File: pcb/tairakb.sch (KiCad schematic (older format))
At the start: 79 parts, among them SW1 SW_Push, SW10 SW_Push, SW11 SW_Push, SW12 SW_Push, SW13 SW_Push, SW14 SW_Push, SW15 SW_Push, SW16 SW_Push, SW17 SW_Push, SW18 SW_Push, SW19 SW_Push, SW2 SW_Push, SW20 SW_Push, SW20-1 SW_Push, SW21 SW_Push, SW22 SW_Push, SW23 SW_Push, SW24 SW_Push, SW25 SW_Push, SW26 SW_Push, SW27 SW_Push, SW28 SW_Push, SW29 SW_Push, SW3 SW_Push, SW30 SW_Push, SW31 SW_Push, SW32 SW_Push, SW33 SW_Push, SW4 SW_Push, SW5 SW_Push, SW6 SW_Push, SW7 SW_Push, SW8 SW_Push, SW9 SW_Push, U3 nice!nano

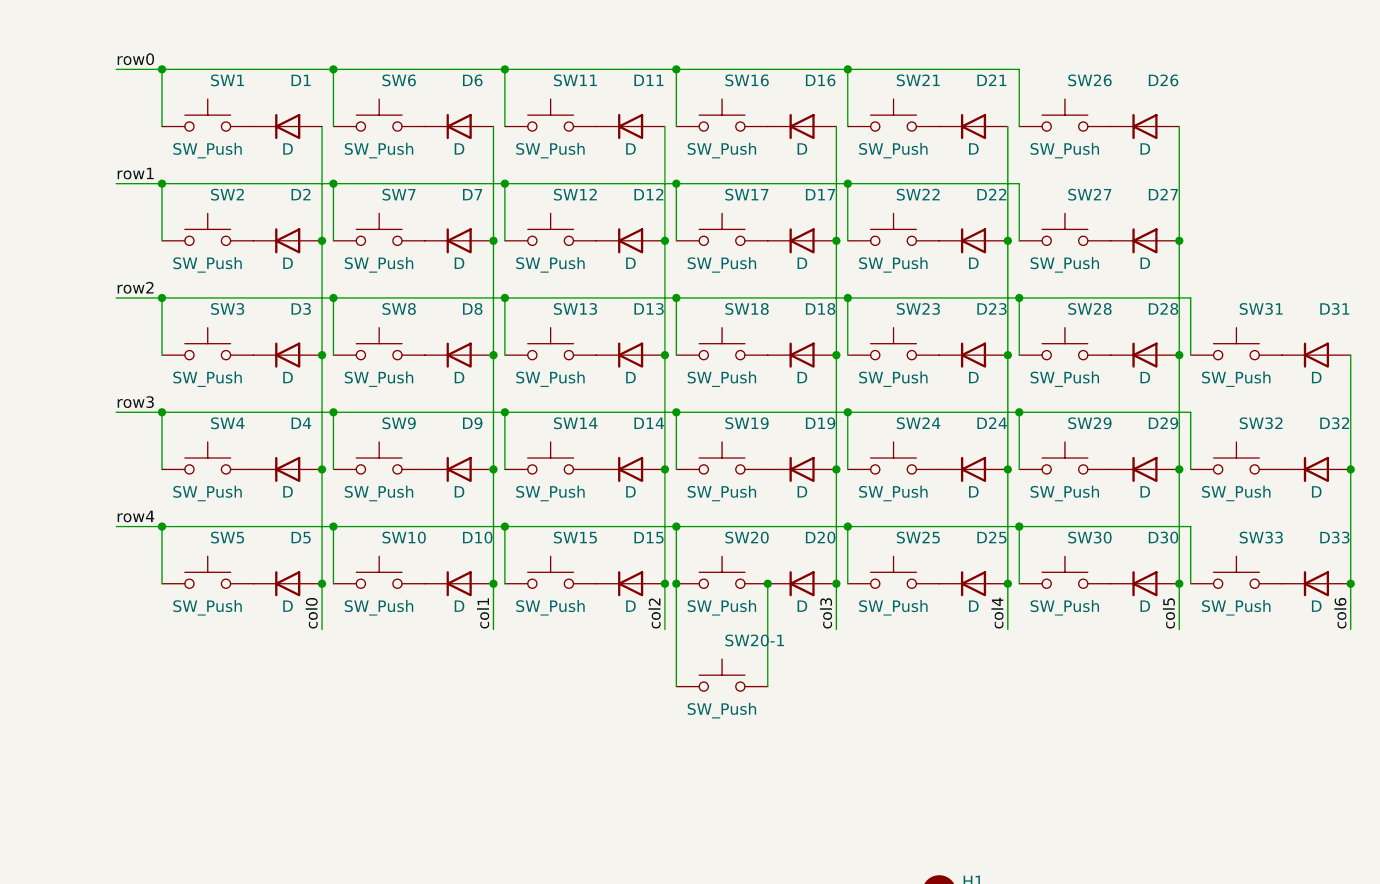
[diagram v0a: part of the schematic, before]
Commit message: Add traces routed by hand
Previously the diodes were connected from the columns to the switches.
Both the ErgoDash and the Corne have them behind the switches connected
to the rows. Since I positioned the diodes on the PCB like they are in
the ErgoDash and Corne, the routing was much more difficult than intended.

This moves the diodes behind the switches and also moves them around a
bit on the PCB. This allowed me to hand route all traces easily, so this
time no autorouter has been involved.

The via count is rather large (156). I opted to rather have ONE trace
and then interconnect each component with vias itself. An alternative
could be to run traces for rows and columns on both layers, but then
there still would be a lot of conflicting paths requiring vias anyway.

I also removed both GND zones. There is nothing on the board that needs
ground except the nice!nano and the battery and I didn't want to start
adding complicated routing just to get GND zones on the whole board. I
left one GND zone in the nice!nano area since it seems reasonable there.
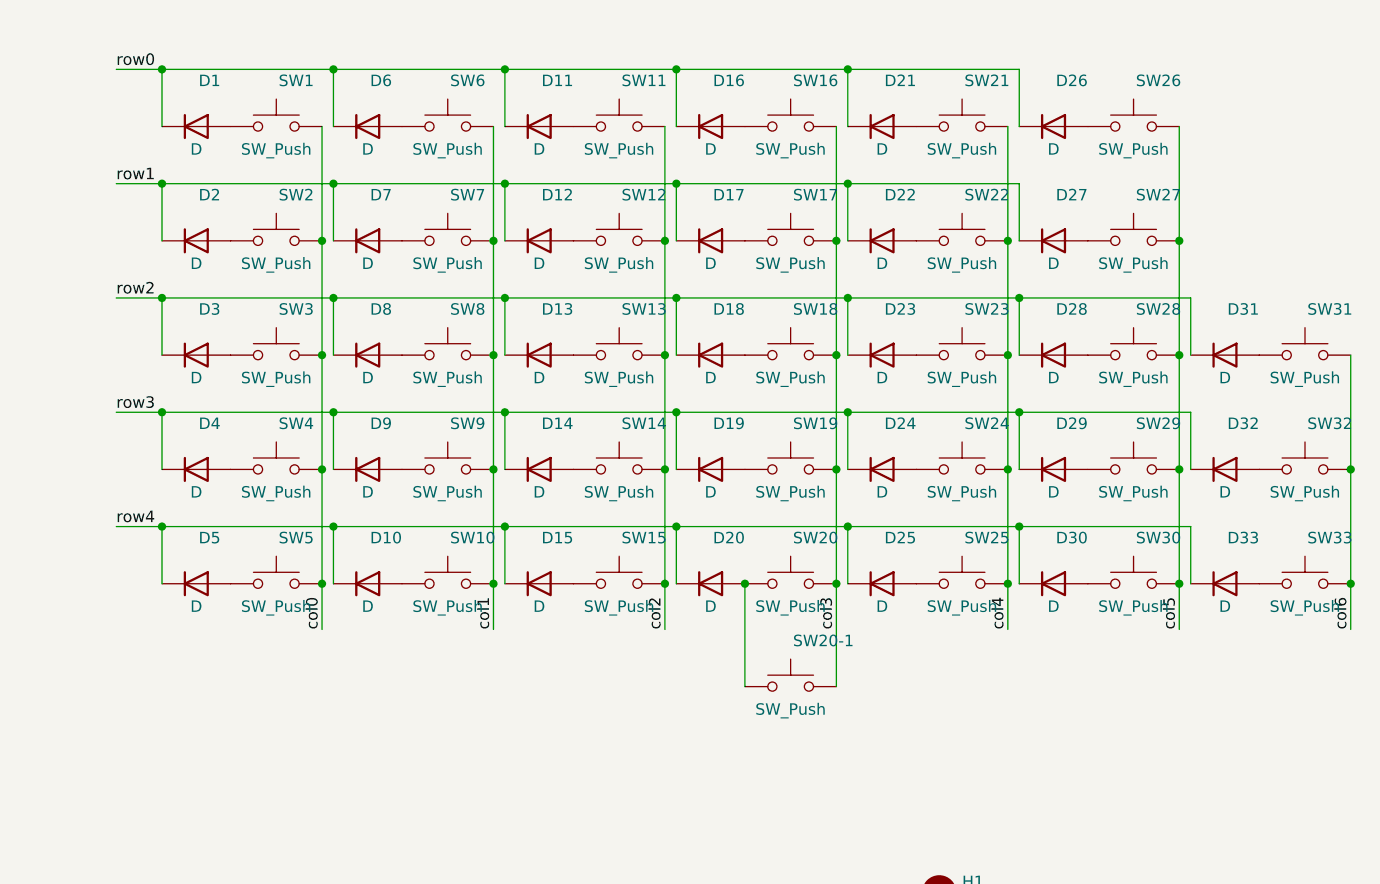
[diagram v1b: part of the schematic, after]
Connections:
- net col0: now also SW1.2, SW2.2, SW3.2, SW4.2, SW5.2; no longer D1.2 (A), D2.2 (A), D3.2 (A), D4.2 (A), D5.2 (A)
- net col1: now also SW10.2, SW6.2, SW7.2, SW8.2, SW9.2; no longer D10.2 (A), D6.2 (A), D7.2 (A), D8.2 (A), D9.2 (A)
- net col2: now also SW11.2, SW12.2, SW13.2, SW14.2, SW15.2; no longer D11.2 (A), D12.2 (A), D13.2 (A), D14.2 (A), D15.2 (A)
- net col3: now also SW16.2, SW17.2, SW18.2, SW19.2, SW20-1.2, SW20.2; no longer D16.2 (A), D17.2 (A), D18.2 (A), D19.2 (A), D20.2 (A)
- net col4: now also SW21.2, SW22.2, SW23.2, SW24.2, SW25.2; no longer D21.2 (A), D22.2 (A), D23.2 (A), D24.2 (A), D25.2 (A)
- net col5: now also SW26.2, SW27.2, SW28.2, SW29.2, SW30.2; no longer D26.2 (A), D27.2 (A), D28.2 (A), D29.2 (A), D30.2 (A)
- net col6: now also SW31.2, SW32.2, SW33.2; no longer D31.2 (A), D32.2 (A), D33.2 (A)
- net row0: now also D1.1 (K), D11.1 (K), D16.1 (K), D21.1 (K), D26.1 (K), D6.1 (K); no longer SW1.1, SW11.1, SW16.1, SW21.1, SW26.1, SW6.1
- net row1: now also D12.1 (K), D17.1 (K), D2.1 (K), D22.1 (K), D27.1 (K), D7.1 (K); no longer SW12.1, SW17.1, SW2.1, SW22.1, SW27.1, SW7.1
- net row2: now also D13.1 (K), D18.1 (K), D23.1 (K), D28.1 (K), D3.1 (K), D31.1 (K), D8.1 (K); no longer SW13.1, SW18.1, SW23.1, SW28.1, SW3.1, SW31.1, SW8.1
- net row3: now also D14.1 (K), D19.1 (K), D24.1 (K), D29.1 (K), D32.1 (K), D4.1 (K), D9.1 (K); no longer SW14.1, SW19.1, SW24.1, SW29.1, SW32.1, SW4.1, SW9.1
- net row4: now also D10.1 (K), D15.1 (K), D20.1 (K), D25.1 (K), D30.1 (K), D33.1 (K), D5.1 (K); no longer SW10.1, SW15.1, SW20-1.1, SW20.1, SW25.1, SW30.1, SW33.1, SW5.1
- new net: D1.2 (A), SW1.1
- new net: D6.2 (A), SW6.1
- new net: D11.2 (A), SW11.1
- new net: D16.2 (A), SW16.1
- new net: D21.2 (A), SW21.1
- new net: D26.2 (A), SW26.1
- new net: D2.2 (A), SW2.1
- new net: D7.2 (A), SW7.1
- new net: D12.2 (A), SW12.1
- new net: D17.2 (A), SW17.1
- new net: D22.2 (A), SW22.1
- new net: D27.2 (A), SW27.1
- new net: D3.2 (A), SW3.1
- new net: D8.2 (A), SW8.1
- new net: D13.2 (A), SW13.1
- new net: D18.2 (A), SW18.1
- new net: D23.2 (A), SW23.1
- new net: D28.2 (A), SW28.1
- new net: D31.2 (A), SW31.1
- new net: D4.2 (A), SW4.1
- new net: D9.2 (A), SW9.1
- new net: D14.2 (A), SW14.1
- new net: D19.2 (A), SW19.1
- new net: D24.2 (A), SW24.1
- new net: D29.2 (A), SW29.1
- new net: D32.2 (A), SW32.1
- new net: D5.2 (A), SW5.1
- new net: D10.2 (A), SW10.1
- new net: D15.2 (A), SW15.1
- new net: D20.2 (A), SW20-1.1, SW20.1
- new net: D25.2 (A), SW25.1
- new net: D30.2 (A), SW30.1
- new net: D33.2 (A), SW33.1
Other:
- moved on the sheet: D1, D10, D11, D12, D13, D14, D15, D16, D17, D18, D19, D2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

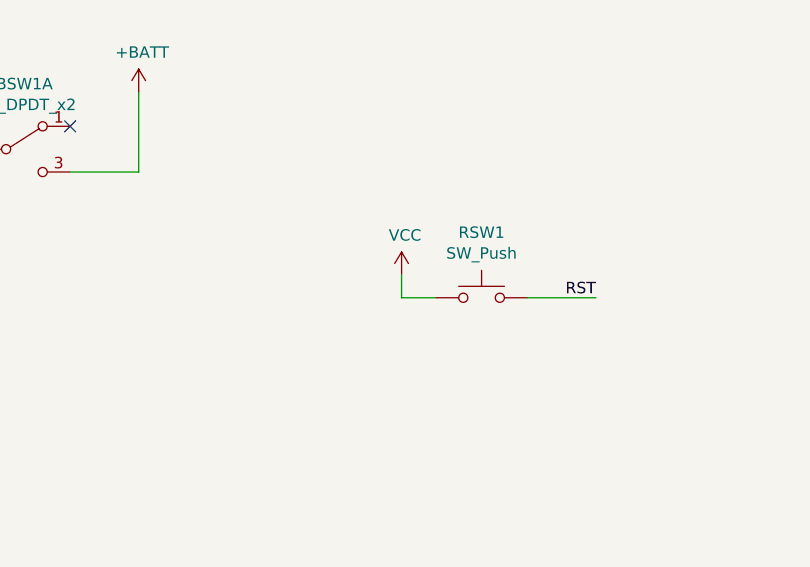
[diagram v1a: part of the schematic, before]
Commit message: Add revision 1.0
Pretty much everything changed. A lot of things were fixed, plates were
added and the spacing between the keys is now 1mm (there was no spacing
before).
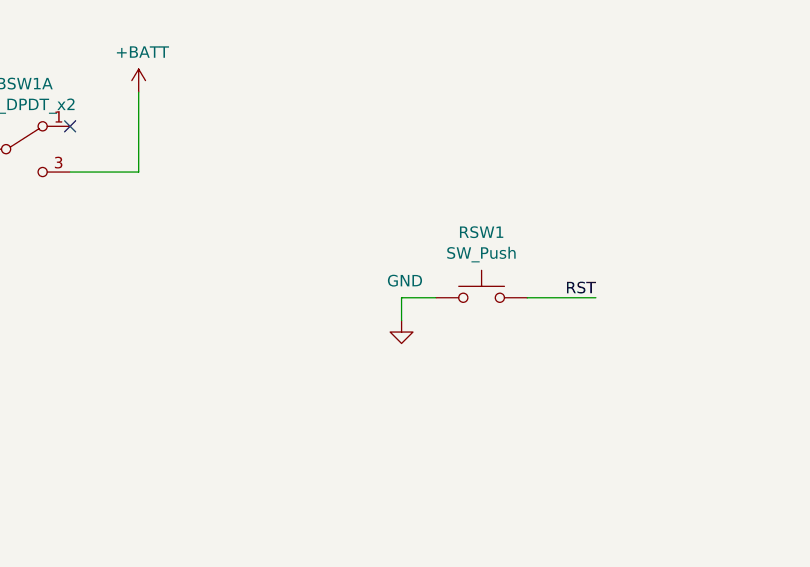
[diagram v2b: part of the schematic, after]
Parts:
- D1, D10, D11, D12, D13, D14, D15, D16, D17, D18, D19, D2, D20, D21, D22, D23, D24, D25, D26, D27, D28, D29, D3, D30, D31, D32, D33, D4, D5, D6, D7, D8, D9: footprint kbd:D3_SMD -> tairakb:D3_SMD
- RSW1: footprint kbd:ResetSW -> tairakb:ResetSW
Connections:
- net GND: now also RSW1.1
- net VCC: no longer RSW1.1
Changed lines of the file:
@@
 Sheet 1 1
 Title "Taira Keyboard"
-Date "2021-09-09"
-Rev "1.0"
+Date "2021-11-03"
+Rev "1.1"
 Comp "strayer | Sven Grunewaldt <sven@grunewaldt.de>"
 Comment1 "A low profile split mechanical keyboard based on the ErgoDash and Corne Chocolate"
@@
 F 0 "RSW1" H 3700 3535 50  0000 C CNN
 F 1 "SW_Push" H 3700 3444 50  0000 C CNN
-F 2 "kbd:ResetSW" H 3700 3450 50  0001 C CNN
+F 2 "tairakb:ResetSW" H 3700 3450 50  0001 C CNN
 F 3 "~" H 3700 3450 50  0001 C CNN
 	1    3700 3250
@@
 F 0 "D1" H 5760 1400 50  0000 L CNN
 F 1 "D" H 5750 1100 50  0000 C CNN
-F 2 "kbd:D3_SMD" H 5750 1400 50  0001 C CNN
+F 2 "tairakb:D3_SMD" H 5750 1400 50  0001 C CNN
 F 3 "" H 5750 1400 50  0001 C CNN
 	1    5750 1200
@@
 F 0 "D6" H 6510 1400 50  0000 L CNN
 F 1 "D" H 6500 1100 50  0000 C CNN
-F 2 "kbd:D3_SMD" H 6500 1400 50  0001 C CNN
+F 2 "tairakb:D3_SMD" H 6500 1400 50  0001 C CNN
 F 3 "" H 6500 1400 50  0001 C CNN
 	1    6500 1200
@@
 F 0 "D11" H 7260 1400 50  0000 L CNN
 F 1 "D" H 7250 1100 50  0000 C CNN
-F 2 "kbd:D3_SMD" H 7250 1400 50  0001 C CNN
+F 2 "tairakb:D3_SMD" H 7250 1400 50  0001 C CNN
 F 3 "" H 7250 1400 50  0001 C CNN
 	1    7250 1200
@@
 F 0 "D16" H 8010 1400 50  0000 L CNN
 F 1 "D" H 8000 1100 50  0000 C CNN
-F 2 "kbd:D3_SMD" H 8000 1400 50  0001 C CNN
+F 2 "tairakb:D3_SMD" H 8000 1400 50  0001 C CNN
 F 3 "" H 8000 1400 50  0001 C CNN
 	1    8000 1200
@@
 F 0 "D21" H 8760 1400 50  0000 L CNN
 F 1 "D" H 8750 1100 50  0000 C CNN
-F 2 "kbd:D3_SMD" H 8750 1400 50  0001 C CNN
+F 2 "tairakb:D3_SMD" H 8750 1400 50  0001 C CNN
 F 3 "" H 8750 1400 50  0001 C CNN
 	1    8750 1200
@@
 F 0 "D26" H 9510 1400 50  0000 L CNN
 F 1 "D" H 9500 1100 50  0000 C CNN
-F 2 "kbd:D3_SMD" H 9500 1400 50  0001 C CNN
+F 2 "tairakb:D3_SMD" H 9500 1400 50  0001 C CNN
 F 3 "" H 9500 1400 50  0001 C CNN
 	1    9500 1200
@@
 F 0 "D2" H 5760 1900 50  0000 L CNN
 F 1 "D" H 5750 1600 50  0000 C CNN
-F 2 "kbd:D3_SMD" H 5750 1900 50  0001 C CNN
+F 2 "tairakb:D3_SMD" H 5750 1900 50  0001 C CNN
 F 3 "" H 5750 1900 50  0001 C CNN
 	1    5750 1700
@@
 F 0 "D7" H 6510 1900 50  0000 L CNN
 F 1 "D" H 6500 1600 50  0000 C CNN
-F 2 "kbd:D3_SMD" H 6500 1900 50  0001 C CNN
+F 2 "tairakb:D3_SMD" H 6500 1900 50  0001 C CNN
 F 3 "" H 6500 1900 50  0001 C CNN
 	1    6500 1700
@@
 F 0 "D12" H 7260 1900 50  0000 L CNN
 F 1 "D" H 7250 1600 50  0000 C CNN
-F 2 "kbd:D3_SMD" H 7250 1900 50  0001 C CNN
+F 2 "tairakb:D3_SMD" H 7250 1900 50  0001 C CNN
 F 3 "" H 7250 1900 50  0001 C CNN
 	1    7250 1700
@@
 F 0 "D17" H 8010 1900 50  0000 L CNN
 F 1 "D" H 8000 1600 50  0000 C CNN
-F 2 "kbd:D3_SMD" H 8000 1900 50  0001 C CNN
+F 2 "tairakb:D3_SMD" H 8000 1900 50  0001 C CNN
 F 3 "" H 8000 1900 50  0001 C CNN
 	1    8000 1700
@@
 F 0 "D22" H 8760 1900 50  0000 L CNN
 F 1 "D" H 8750 1600 50  0000 C CNN
-F 2 "kbd:D3_SMD" H 8750 1900 50  0001 C CNN
+F 2 "tairakb:D3_SMD" H 8750 1900 50  0001 C CNN
 F 3 "" H 8750 1900 50  0001 C CNN
 	1    8750 1700
@@
 F 0 "D27" H 9510 1900 50  0000 L CNN
 F 1 "D" H 9500 1600 50  0000 C CNN
-F 2 "kbd:D3_SMD" H 9500 1900 50  0001 C CNN
+F 2 "tairakb:D3_SMD" H 9500 1900 50  0001 C CNN
 F 3 "" H 9500 1900 50  0001 C CNN
 	1    9500 1700
@@
 F 0 "D3" H 5760 2400 50  0000 L CNN
 F 1 "D" H 5750 2100 50  0000 C CNN
-F 2 "kbd:D3_SMD" H 5750 2400 50  0001 C CNN
+F 2 "tairakb:D3_SMD" H 5750 2400 50  0001 C CNN
 F 3 "" H 5750 2400 50  0001 C CNN
 	1    5750 2200
@@
 F 0 "D8" H 6510 2400 50  0000 L CNN
 F 1 "D" H 6500 2100 50  0000 C CNN
-F 2 "kbd:D3_SMD" H 6500 2400 50  0001 C CNN
+F 2 "tairakb:D3_SMD" H 6500 2400 50  0001 C CNN
 F 3 "" H 6500 2400 50  0001 C CNN
 	1    6500 2200
@@
 F 0 "D13" H 7260 2400 50  0000 L CNN
 F 1 "D" H 7250 2100 50  0000 C CNN
-F 2 "kbd:D3_SMD" H 7250 2400 50  0001 C CNN
+F 2 "tairakb:D3_SMD" H 7250 2400 50  0001 C CNN
 F 3 "" H 7250 2400 50  0001 C CNN
 	1    7250 2200
@@
 F 0 "D18" H 8010 2400 50  0000 L CNN
 F 1 "D" H 8000 2100 50  0000 C CNN
-F 2 "kbd:D3_SMD" H 8000 2400 50  0001 C CNN
+F 2 "tairakb:D3_SMD" H 8000 2400 50  0001 C CNN
 F 3 "" H 8000 2400 50  0001 C CNN
 	1    8000 2200
@@
 F 0 "D23" H 8760 2400 50  0000 L CNN
 F 1 "D" H 8750 2100 50  0000 C CNN
-F 2 "kbd:D3_SMD" H 8750 2400 50  0001 C CNN
+F 2 "tairakb:D3_SMD" H 8750 2400 50  0001 C CNN
 F 3 "" H 8750 2400 50  0001 C CNN
 	1    8750 2200
@@
 F 0 "D28" H 9510 2400 50  0000 L CNN
 F 1 "D" H 9500 2100 50  0000 C CNN
-F 2 "kbd:D3_SMD" H 9500 2400 50  0001 C CNN
+F 2 "tairakb:D3_SMD" H 9500 2400 50  0001 C CNN
 F 3 "" H 9500 2400 50  0001 C CNN
 	1    9500 2200
@@
 F 0 "D31" H 10260 2400 50  0000 L CNN
 F 1 "D" H 10250 2100 50  0000 C CNN
-F 2 "kbd:D3_SMD" H 10250 2400 50  0001 C CNN
+F 2 "tairakb:D3_SMD" H 10250 2400 50  0001 C CNN
 F 3 "" H 10250 2400 50  0001 C CNN
 	1    10250 2200
@@
 F 0 "D4" H 5760 2900 50  0000 L CNN
 F 1 "D" H 5750 2600 50  0000 C CNN
-F 2 "kbd:D3_SMD" H 5750 2900 50  0001 C CNN
+F 2 "tairakb:D3_SMD" H 5750 2900 50  0001 C CNN
 F 3 "" H 5750 2900 50  0001 C CNN
 	1    5750 2700
@@
 F 0 "D9" H 6510 2900 50  0000 L CNN
 F 1 "D" H 6500 2600 50  0000 C CNN
-F 2 "kbd:D3_SMD" H 6500 2900 50  0001 C CNN
+F 2 "tairakb:D3_SMD" H 6500 2900 50  0001 C CNN
 F 3 "" H 6500 2900 50  0001 C CNN
 	1    6500 2700
@@
 F 0 "D14" H 7260 2900 50  0000 L CNN
 F 1 "D" H 7250 2600 50  0000 C CNN
-F 2 "kbd:D3_SMD" H 7250 2900 50  0001 C CNN
+F 2 "tairakb:D3_SMD" H 7250 2900 50  0001 C CNN
 F 3 "" H 7250 2900 50  0001 C CNN
 	1    7250 2700
@@
 F 0 "D19" H 8010 2900 50  0000 L CNN
 F 1 "D" H 8000 2600 50  0000 C CNN
-F 2 "kbd:D3_SMD" H 8000 2900 50  0001 C CNN
+F 2 "tairakb:D3_SMD" H 8000 2900 50  0001 C CNN
 F 3 "" H 8000 2900 50  0001 C CNN
 	1    8000 2700
@@
 F 0 "D24" H 8760 2900 50  0000 L CNN
 F 1 "D" H 8750 2600 50  0000 C CNN
-F 2 "kbd:D3_SMD" H 8750 2900 50  0001 C CNN
+F 2 "tairakb:D3_SMD" H 8750 2900 50  0001 C CNN
 F 3 "" H 8750 2900 50  0001 C CNN
 	1    8750 2700
@@
 F 0 "D29" H 9510 2900 50  0000 L CNN
 F 1 "D" H 9500 2600 50  0000 C CNN
-F 2 "kbd:D3_SMD" H 9500 2900 50  0001 C CNN
+F 2 "tairakb:D3_SMD" H 9500 2900 50  0001 C CNN
 F 3 "" H 9500 2900 50  0001 C CNN
 	1    9500 2700
@@
 F 0 "D32" H 10260 2900 50  0000 L CNN
 F 1 "D" H 10250 2600 50  0000 C CNN
-F 2 "kbd:D3_SMD" H 10250 2900 50  0001 C CNN
+F 2 "tairakb:D3_SMD" H 10250 2900 50  0001 C CNN
 F 3 "" H 10250 2900 50  0001 C CNN
 	1    10250 2700
@@
 F 0 "D5" H 5760 3400 50  0000 L CNN
 F 1 "D" H 5750 3100 50  0000 C CNN
-F 2 "kbd:D3_SMD" H 5750 3400 50  0001 C CNN
+F 2 "tairakb:D3_SMD" H 5750 3400 50  0001 C CNN
 F 3 "" H 5750 3400 50  0001 C CNN
 	1    5750 3200
@@
 F 0 "D10" H 6510 3400 50  0000 L CNN
 F 1 "D" H 6500 3100 50  0000 C CNN
-F 2 "kbd:D3_SMD" H 6500 3400 50  0001 C CNN
+F 2 "tairakb:D3_SMD" H 6500 3400 50  0001 C CNN
 F 3 "" H 6500 3400 50  0001 C CNN
 	1    6500 3200
@@
 F 0 "D15" H 7260 3400 50  0000 L CNN
 F 1 "D" H 7250 3100 50  0000 C CNN
-F 2 "kbd:D3_SMD" H 7250 3400 50  0001 C CNN
+F 2 "tairakb:D3_SMD" H 7250 3400 50  0001 C CNN
 F 3 "" H 7250 3400 50  0001 C CNN
 	1    7250 3200
@@
 F 0 "D20" H 8010 3400 50  0000 L CNN
 F 1 "D" H 8000 3100 50  0000 C CNN
-F 2 "kbd:D3_SMD" H 8000 3400 50  0001 C CNN
+F 2 "tairakb:D3_SMD" H 8000 3400 50  0001 C CNN
 F 3 "" H 8000 3400 50  0001 C CNN
 	1    8000 3200
@@
 F 0 "D25" H 8760 3400 50  0000 L CNN
 F 1 "D" H 8750 3100 50  0000 C CNN
-F 2 "kbd:D3_SMD" H 8750 3400 50  0001 C CNN
+F 2 "tairakb:D3_SMD" H 8750 3400 50  0001 C CNN
 F 3 "" H 8750 3400 50  0001 C CNN
 	1    8750 3200
@@
 F 0 "D30" H 9510 3400 50  0000 L CNN
 F 1 "D" H 9500 3100 50  0000 C CNN
-F 2 "kbd:D3_SMD" H 9500 3400 50  0001 C CNN
+F 2 "tairakb:D3_SMD" H 9500 3400 50  0001 C CNN
 F 3 "" H 9500 3400 50  0001 C CNN
 	1    9500 3200
@@
 F 0 "D33" H 10260 3400 50  0000 L CNN
 F 1 "D" H 10250 3100 50  0000 C CNN
-F 2 "kbd:D3_SMD" H 10250 3400 50  0001 C CNN
+F 2 "tairakb:D3_SMD" H 10250 3400 50  0001 C CNN
 F 3 "" H 10250 3400 50  0001 C CNN
 	1    10250 3200
@@
 Wire Wire Line
 	2200 2700 2200 2350
-Wire Wire Line
-	3500 3250 3350 3250
-Wire Wire Line
-	3350 3250 3350 3150
-$Comp
-L power:VCC #PWR0108
+$Comp
+L power:GND #PWR0108
 U 1 1 609500C7
-P 3350 3150
-F 0 "#PWR0108" H 3350 3000 50  0001 C CNN
-F 1 "VCC" H 3365 3323 50  0000 C CNN
-F 2 "" H 3350 3150 50  0001 C CNN
-F 3 "" H 3350 3150 50  0001 C CNN
-	1    3350 3150
+P 3350 3350
+F 0 "#PWR0108" H 3350 3200 50  0001 C CNN
+F 1 "GND" H 3365 3523 50  0000 C CNN
+F 2 "" H 3350 3350 50  0001 C CNN
+F 3 "" H 3350 3350 50  0001 C CNN
+	1    3350 3350
 	1    0    0    -1
 $EndComp
@@
 	8150 3200 8150 3650
 Connection ~ 8150 3200
+Wire Wire Line
+	3500 3250 3350 3250
+Wire Wire Line
+	3350 3250 3350 3350
 $EndSCHEMATC
